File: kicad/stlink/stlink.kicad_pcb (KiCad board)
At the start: 2 copper layers, 50.5 x 34 mm, 42 parts, among them J1 USB_Micro, J2 MCU_FLASHING, J3 DEBUG, Q1 9013, U1 LD3985M33R_SOT23, U2 STM32F103CBTx, Y1 Crystal

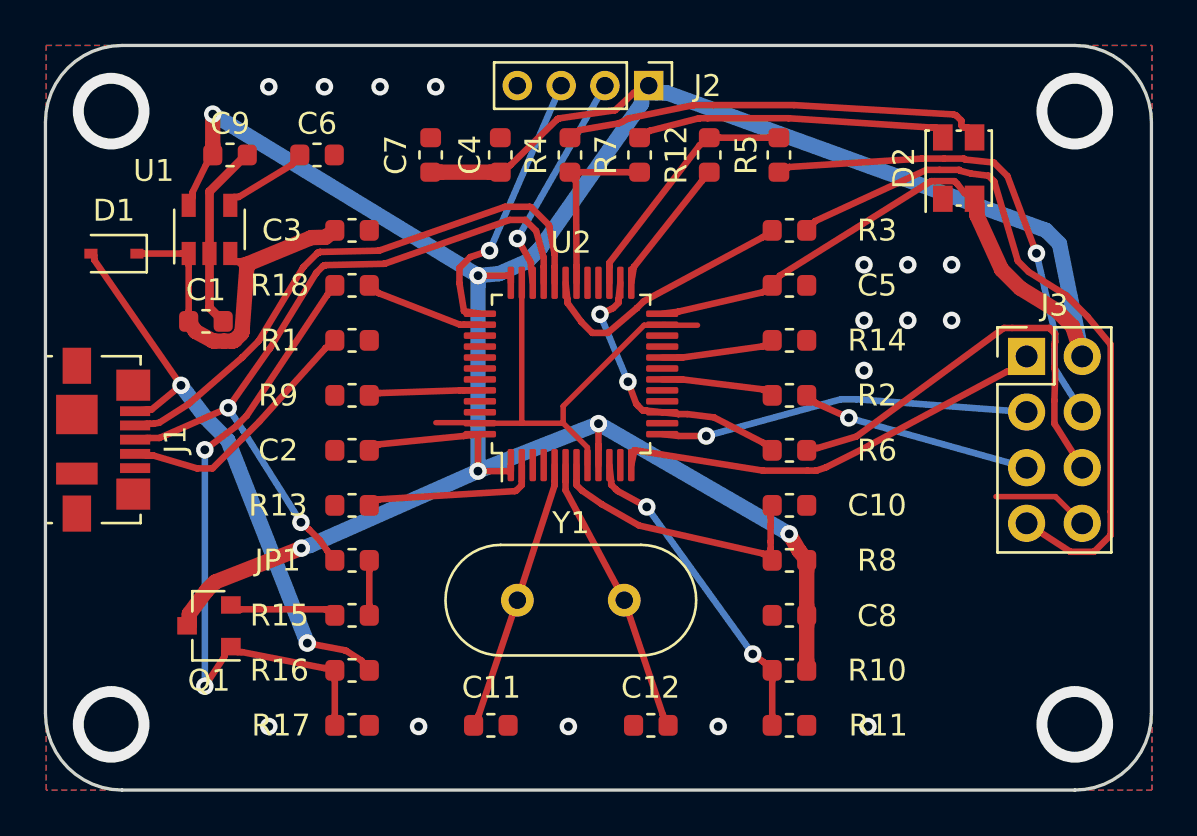
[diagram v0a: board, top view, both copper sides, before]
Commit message: sch + pcb update
Updated schematics:
* Added ESD protection for USB
* Added notes and comments to schematics
* Added BOM
Updated PCB:
* Slightly changed layout
* Rerouted connections
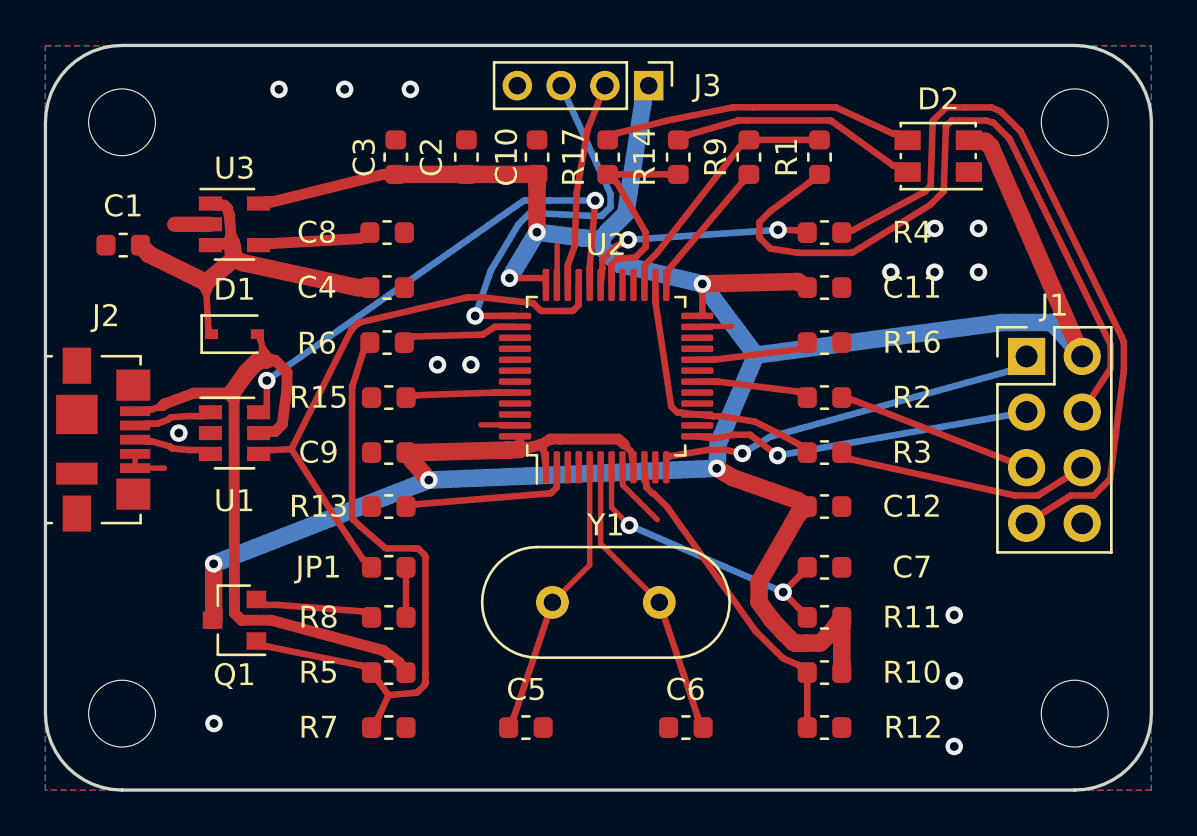
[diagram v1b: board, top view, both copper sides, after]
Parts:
- removed G***: LOGO, custom_logos:keep_on
- removed G***: github, custom_logos:qr_stlink
- removed the R1 at (64.0, 115.5)
- removed the R15 at (64.0, 128.0)
- removed R18: 22, Resistor_SMD:R_0603_1608Metric
- added G1: LOGO, custom_logos:qr_stlink_v2, B.Cu at (63.3, 127.1)
- added G2: LOGO, custom_logos:keep_on, B.Cu at (75.5, 116.5)
- added R6: 22, Resistor_SMD:R_0603_1608Metric, F.Cu at (65.6, 115.6)
- added R8: 1k5, Resistor_SMD:R_0603_1608Metric, F.Cu at (65.7, 128.1)
- added U1: USBLC6-2SC6, Package_TO_SOT_SMD:SOT-23-6, F.Cu at (58.6, 119.7)
- C9: renamed from C2; value 100nF -> 1uF
- JP1: value SolderJumper_2_Open -> Solder bridge
- Q1: value 9013 -> KTC9013S
- Y1: footprint Crystal:Crystal_HC49-4H_Vertical -> Crystal:Crystal_HC49-U_Vertical
- moved C3 7.57 mm to (66.0, 107.1), turned to 90 degrees
- moved D1 6.62 mm to (58.6, 115.2), turned to 0 degrees
- moved C12 5.22 mm to (85.6, 123.1), turned to 0 degrees
- moved C1 5.14 mm to (53.6, 111.1), turned to 180 degrees
- moved C8 4.78 mm to (65.6, 110.5)
- moved C7 3.25 mm to (85.6, 125.8)
- moved C4 3.06 mm to (65.6, 113.1)
- moved R11 3.06 mm to (85.6, 128.1)
- moved R1 1.86 mm to (85.3, 107.1)
- moved R9 1.81 mm to (82.1, 107.1)
- moved R14 1.77 mm to (78.9, 107.1)
- moved R17 1.72 mm to (75.7, 107.1)
- moved JP1 1.71 mm to (65.7, 125.8)
- moved C10 1.68 mm to (72.4, 107.1)
- moved R7 1.68 mm to (65.7, 133.1)
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- renumbered C4 to C10, C5 to C11, C8 to C12, C7 to C2, C9 to C3, C3 to C4, C11 to C5, C12 to C6, C10 to C7, C6 to C8, J3 to J1, J1 to J2, J2 to J3, R5 to R1, R8 to R11, R11 to R12, R7 to R14, R9 to R15, R14 to R16, R4 to R17, R6 to R3, R3 to R4, R16 to R5, R17 to R7, R12 to R9, U1 to U3
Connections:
- J2 pad 2: /USB_DM -> /D-
- J2 pad 3: /USB_DP -> /D+
- J2 pad 4: Net-(J1-Pad4) (its old number) -> GND
- U2 pad 11: Net-(U2-Pad11) -> (no net)
- U2 pad 14: Net-(U2-Pad14) -> (no net)
- U2 pad 16: Net-(U2-Pad16) -> (no net)
- U2 pad 17: Net-(U2-Pad17) -> (no net)
- U2 pad 19: Net-(U2-Pad19) -> (no net)
- U2 pad 21: Net-(U2-Pad21) -> (no net)
- U2 pad 22: Net-(U2-Pad22) -> (no net)
- U2 pad 28: Net-(U2-Pad28) -> (no net)
- U2 pad 29: Net-(U2-Pad29) -> (no net)
- U2 pad 3: Net-(U2-Pad3) -> (no net)
- U2 pad 39: Net-(U2-Pad39) -> (no net)
- U2 pad 4: Net-(U2-Pad4) -> (no net)
- U2 pad 40: Net-(U2-Pad40) -> (no net)
- U2 pad 41: Net-(U2-Pad41) -> (no net)
- U2 pad 42: Net-(U2-Pad42) -> (no net)
- U2 pad 43: Net-(U2-Pad43) -> (no net)
- U2 pad 45: Net-(U2-Pad45) -> (no net)
- U2 pad 46: Net-(U2-Pad46) -> (no net)
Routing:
- net GND: track 36.2 -> 11.7 mm, vias 16 -> 15
- net +3V3: track 152.4 -> 140.0 mm
- net Net-(J1-Pad4) (its old number): track 11.7 -> 0.00 mm
- net Net-(J1-Pad4): track 22.3 -> 34.0 mm, vias 1 -> 0
- net +5V: track 26.3 -> 34.7 mm, vias 2 -> 0
- net Net-(J1-Pad6): track 19.7 -> 11.6 mm
- net /USB_DP: track 33.6 -> 26.0 mm, vias 2 -> 0
- net Net-(D2-Pad3): track 19.4 -> 14.3 mm
- net /SWCLK: track 12.6 -> 17.1 mm
- net /D-: track 0.00 -> 3.56 mm
- net /D+: track 0.00 -> 3.55 mm
- net Net-(C1-Pad1): track 17.6 -> 20.5 mm
- net Net-(D2-Pad2): track 14.3 -> 11.4 mm
- net /USB_DM: track 25.8 -> 23.1 mm, vias 0 -> 2
- net /TX: track 20.1 -> 17.9 mm, vias 0 -> 1
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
